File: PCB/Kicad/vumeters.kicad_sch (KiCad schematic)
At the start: 80 parts

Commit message: update elements WIP
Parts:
- D1, D10, D11, D12, D13, D14, D15, D16, D17, D18, D19, D2, D20, D21, D22, D23, D24, D25, D26, D27, D28, D29, D3, D30, D31, D32, D33, D34, D35, D36, D37, D38, D39, D4, D40, D5, D6, D7, D8, D9: renamed from D?; symbol Traktorino-rescue:LED_ALT-Device -> Device:LED_Filled
- gave numbers to parts that had none: 40
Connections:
- net GND: now also D1.1 (K), D10.1 (K), D11.1 (K), D12.1 (K), D13.1 (K), D14.1 (K), D15.1 (K), D16.1 (K), D17.1 (K), D18.1 (K), D19.1 (K), D2.1 (K), D20.1 (K), D21.1 (K), D22.1 (K), D23.1 (K), D24.1 (K), D25.1 (K), D26.1 (K), D27.1 (K), D28.1 (K), D29.1 (K), D3.1 (K), D30.1 (K), D31.1 (K), D32.1 (K), D33.1 (K), D34.1 (K), D35.1 (K), D36.1 (K), D37.1 (K), D38.1 (K), D39.1 (K), D4.1 (K), D40.1 (K), D5.1 (K), D6.1 (K), D7.1 (K), D8.1 (K), D9.1 (K)
- net at R1.2: now also D1.2 (A)
- net at R2.2: now also D2.2 (A)
- net at R3.2: now also D3.2 (A)
- net at R4.2: now also D4.2 (A)
- net at R5.2: now also D5.2 (A)
- net at R6.2: now also D6.2 (A)
- net at R7.2: now also D7.2 (A)
- net at R8.2: now also D8.2 (A)
- net at R16.2: now also D16.2 (A)
- net at R15.2: now also D15.2 (A)
- net at R14.2: now also D14.2 (A)
- net at R13.2: now also D13.2 (A)
- net at R12.2: now also D12.2 (A)
- net at R11.2: now also D11.2 (A)
- net at R10.2: now also D10.2 (A)
- net at R9.2: now also D9.2 (A)
- net at R24.2: now also D24.2 (A)
- net at R23.2: now also D23.2 (A)
- net at R22.2: now also D22.2 (A)
- net at R21.2: now also D21.2 (A)
- net at R20.2: now also D20.2 (A)
- net at R19.2: now also D19.2 (A)
- net at R18.2: now also D18.2 (A)
- net at R17.2: now also D17.2 (A)
- net at R32.2: now also D32.2 (A)
- net at R31.2: now also D31.2 (A)
- net at R30.2: now also D30.2 (A)
- net at R29.2: now also D29.2 (A)
- net at R28.2: now also D28.2 (A)
- net at R27.2: now also D27.2 (A)
- net at R26.2: now also D26.2 (A)
- net at R25.2: now also D25.2 (A)
- net at R40.2: now also D40.2 (A)
- net at R39.2: now also D39.2 (A)
- net at R38.2: now also D38.2 (A)
- net at R37.2: now also D37.2 (A)
- net at R36.2: now also D36.2 (A)
- net at R35.2: now also D35.2 (A)
- net at R34.2: now also D34.2 (A)
- net at R33.2: now also D33.2 (A)

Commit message: progress
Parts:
- added D41, D42, D43, D44, D45, D46, D47: LED_ALT, LED_THT:LED_Rectangular_W3.0mm_H2.0mm, symbol Device:LED_Filled
- added R41, R42, R43, R44, R45, R46, R47: R_Small, Resistor_THT:R_Axial_DIN0207_L6.3mm_D2.5mm_P7.62mm_Horizontal, symbol Device:R_Small
- D1: value LED_ALT -> VUL1-0; footprint (none) -> LED_THT:LED_Rectangular_W3.0mm_H2.0mm
- D10, D11, D12, D13, D14, D15, D16, D9: value LED_ALT -> VUL2; footprint (none) -> LED_THT:LED_Rectangular_W3.0mm_H2.0mm
- D17, D18, D19, D20, D21, D22, D23, D24: value LED_ALT -> VUL3; footprint (none) -> LED_THT:LED_Rectangular_W3.0mm_H2.0mm
- D2: value LED_ALT -> VUL1-1; footprint (none) -> LED_THT:LED_Rectangular_W3.0mm_H2.0mm
- D25, D26, D27, D28, D29, D30, D31, D32: value LED_ALT -> VUMAS-L; footprint (none) -> LED_THT:LED_Rectangular_W3.0mm_H2.0mm
- D3, D4, D5, D6, D7, D8: value LED_ALT -> VUL1-; footprint (none) -> LED_THT:LED_Rectangular_W3.0mm_H2.0mm
- D33, D34, D35, D36, D37, D38, D39, D40: value LED_ALT -> VUMAS-R; footprint (none) -> LED_THT:LED_Rectangular_W3.0mm_H2.0mm
- R1, R10, R11, R12, R13, R14, R15, R16, R17, R18, R19, R2, R20, R21, R22, R23, R24, R25, R26, R27, R28, R29, R3, R30, R31, R32, R33, R34, R35, R36, R37, R38, R39, R4, R40, R5, R6, R7, R8, R9: footprint (none) -> Resistor_THT:R_Axial_DIN0207_L6.3mm_D2.5mm_P7.62mm_Horizontal
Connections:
- net GND: now also D41.1 (K), D42.1 (K), D43.1 (K), D44.1 (K), D45.1 (K), D46.1 (K), D47.1 (K)
- net VULMASL-0 renamed VUMASL-0
- net VULMASL-1 renamed VUMASL-1
- net VULMASL-2 renamed VUMASL-2
- net VULMASL-3 renamed VUMASL-3
- net VULMASL-4 renamed VUMASL-4
- net VULMASL-5 renamed VUMASL-5
- net VULMASL-6 renamed VUMASL-6
- net VULMASL-7 renamed VUMASL-7
- new net: D44.2 (A), R44.2
- new net: D42.2 (A), R42.2
- new net: D47.2 (A), R47.2
- new net: D45.2 (A), R45.2
- new net: D43.2 (A), R43.2
- new net: D46.2 (A), R46.2
- new net: D41.2 (A), R41.2
- new net LEDCUEL: R44.1
- new net LEDCUER: R42.1
- new net LEDHPL1: R47.1
- new net LEDHPL2: R46.1
- new net LEDHPL3: R45.1
- new net LEDPLAYL: R43.1
- new net LEDPLAYR: R41.1
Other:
- moved on the sheet: D1, D10, D11, D12, D13, D14, D15, D16, D17, D18, D19, D2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

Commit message: mod layout
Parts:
- renumbered D42 to D10, D43 to D11, D44 to D12, D9 to D13, D10 to D14, D11 to D15, D12 to D16, D13 to D17, D14 to D18, D15 to D19, D16 to D20, D45 to D21, D46 to D22, D47 to D23, D17 to D24, D18 to D25, D19 to D26, D20 to D27, D21 to D28, D22 to D29, D23 to D30, D24 to D31, D25 to D32, D26 to D33, D27 to D34, D28 to D35, D29 to D36, D30 to D37, D31 to D38, D32 to D39, D33 to D40, D34 to D41, D35 to D42, D36 to D43, D37 to D44, D38 to D45, D39 to D46, D40 to D47, D41 to D9, R42 to R10, R43 to R11, R44 to R12, R9 to R13, R10 to R14, R11 to R15, R12 to R16, R13 to R17, R14 to R18, R15 to R19, R16 to R20, R45 to R21, R46 to R22, R47 to R23, R17 to R24, R18 to R25, R19 to R26, R20 to R27, R21 to R28, R22 to R29, R23 to R30, R24 to R31, R25 to R32, R26 to R33, R27 to R34, R28 to R35, R29 to R36, R30 to R37, R31 to R38, R32 to R39, R33 to R40, R34 to R41, R35 to R42, R36 to R43, R37 to R44, R38 to R45, R39 to R46, R40 to R47, R41 to R9

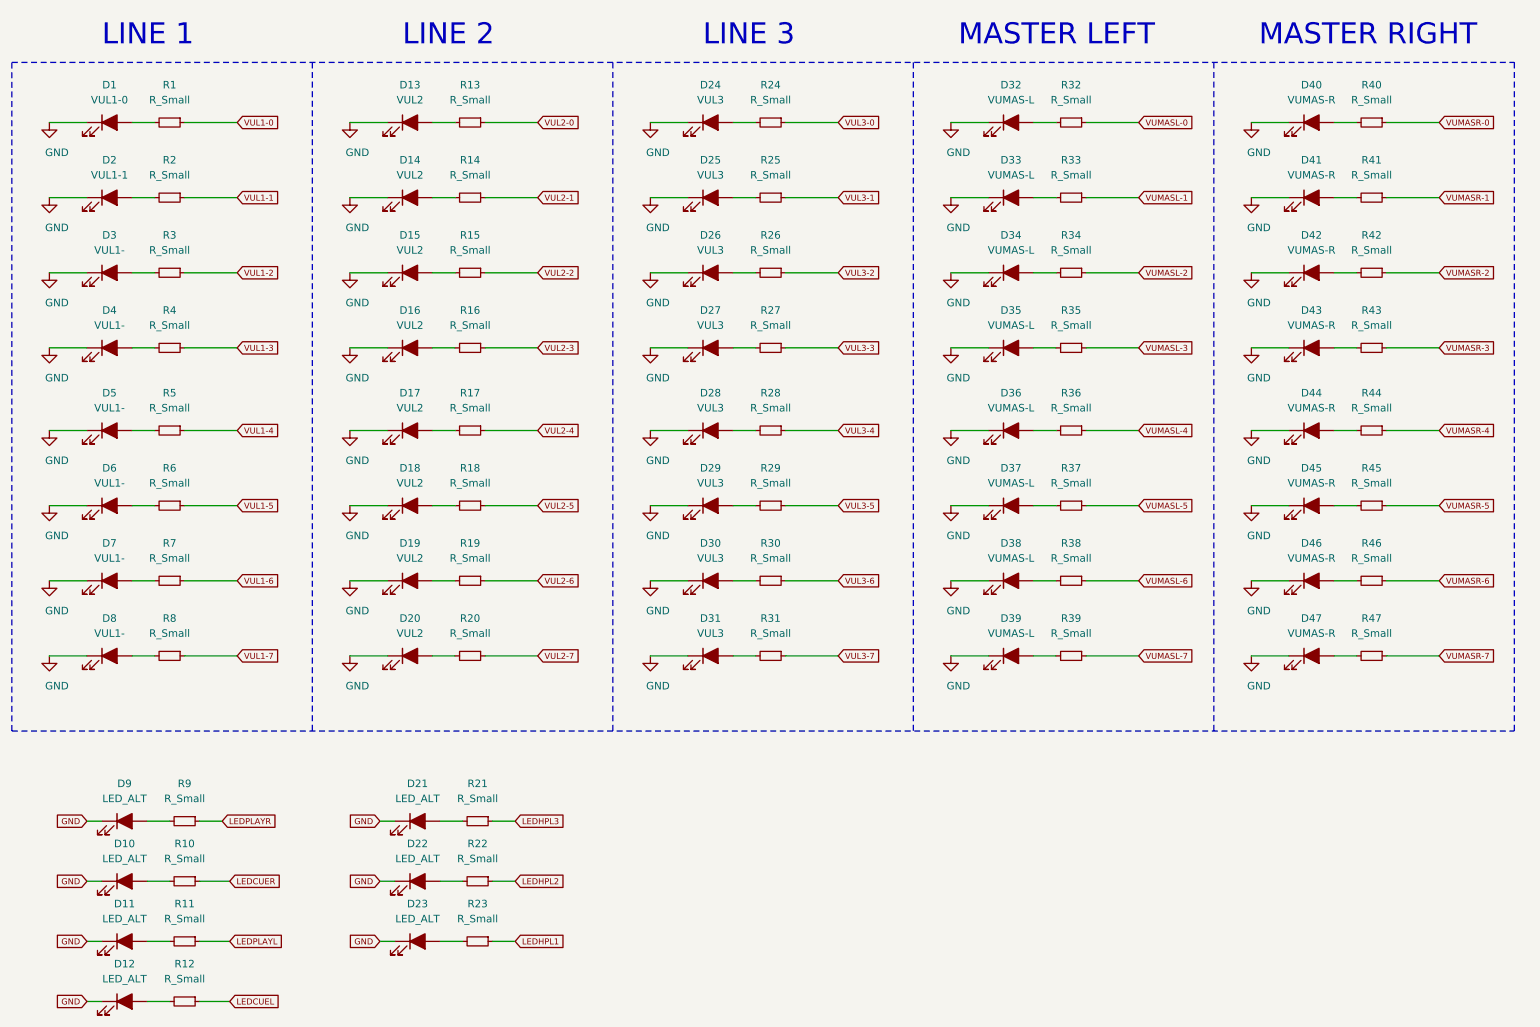
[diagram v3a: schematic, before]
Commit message: Arduino mega retrofit WIP
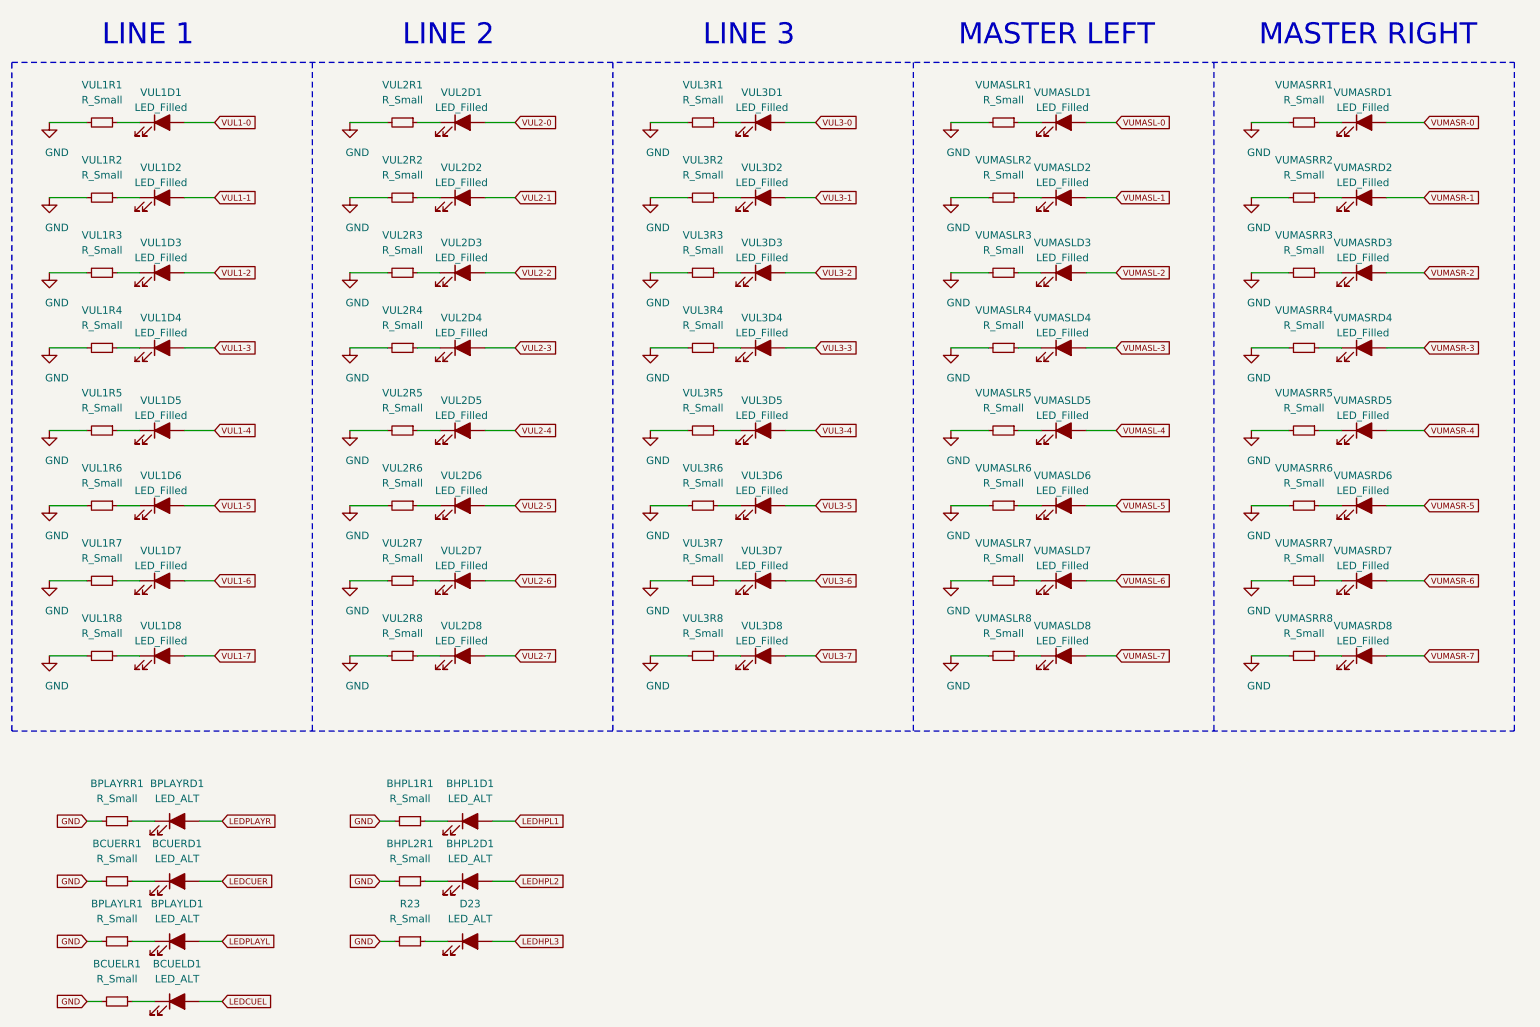
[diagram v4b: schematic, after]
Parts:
- removed D1: VUL1-0, LED_THT:LED_Rectangular_W3.0mm_H2.0mm, symbol Device:LED_Filled
- removed D13, D14, D15, D16, D17, D18, D19, D20: VUL2, LED_THT:LED_Rectangular_W3.0mm_H2.0mm, symbol Device:LED_Filled
- removed D2: VUL1-1, LED_THT:LED_Rectangular_W3.0mm_H2.0mm, symbol Device:LED_Filled
- removed D24, D25, D26, D27, D28, D29, D30, D31: VUL3, LED_THT:LED_Rectangular_W3.0mm_H2.0mm, symbol Device:LED_Filled
- removed D3, D4, D5, D6, D7, D8: VUL1-, LED_THT:LED_Rectangular_W3.0mm_H2.0mm, symbol Device:LED_Filled
- removed D32, D33, D34, D35, D36, D37, D38, D39: VUMAS-L, LED_THT:LED_Rectangular_W3.0mm_H2.0mm, symbol Device:LED_Filled
- removed D40, D41, D42, D43, D44, D45, D46, D47: VUMAS-R, LED_THT:LED_Rectangular_W3.0mm_H2.0mm, symbol Device:LED_Filled
- removed R13, R14, R15, R16, R17, R18, R19, R2, R20, R24, R25, R26, R27, R28, R29, R3, R30, R31, R32, R33, R34, R35, R36, R37, R38, R39, R4, R40, R41, R42, R43, R44, R45, R46, R47, R5, R6, R7, R8: R_Small, Resistor_THT:R_Axial_DIN0207_L6.3mm_D2.5mm_P7.62mm_Horizontal, symbol Device:R_Small
- added VUL1D1, VUL1D2, VUL1D3, VUL1D4, VUL1D5, VUL1D6, VUL1D7, VUL1D8, VUL2D1, VUL2D2, VUL2D3, VUL2D4, VUL2D5, VUL2D6, VUL2D7, VUL2D8, VUL3D1, VUL3D2, VUL3D3, VUL3D4, VUL3D5, VUL3D6, VUL3D7, VUL3D8, VUMASLD1, VUMASLD2, VUMASLD3, VUMASLD4, VUMASLD5, VUMASLD6, VUMASLD7, VUMASLD8, VUMASRD1, VUMASRD2, VUMASRD3, VUMASRD4, VUMASRD5, VUMASRD6, VUMASRD7, VUMASRD8: LED_Filled, LED_THT:LED_Rectangular_W3.0mm_H2.0mm, symbol Device:LED_Filled
- added VUL1R2, VUL1R3, VUL1R4, VUL1R5, VUL1R6, VUL1R7, VUL1R8, VUL2R1, VUL2R2, VUL2R3, VUL2R4, VUL2R5, VUL2R6, VUL2R7, VUL2R8, VUL3R1, VUL3R2, VUL3R3, VUL3R4, VUL3R5, VUL3R6, VUL3R7, VUL3R8, VUMASLR1, VUMASLR2, VUMASLR3, VUMASLR4, VUMASLR5, VUMASLR6, VUMASLR7, VUMASLR8, VUMASRR1, VUMASRR2, VUMASRR3, VUMASRR4, VUMASRR5, VUMASRR6, VUMASRR7, VUMASRR8: R_Small, Resistor_SMD:R_1206_3216Metric_Pad1.30x1.75mm_HandSolder, symbol Device:R_Small
- BCUELR1: renamed from R12; footprint Resistor_THT:R_Axial_DIN0207_L6.3mm_D2.5mm_P7.62mm_Horizontal -> Resistor_SMD:R_1206_3216Metric_Pad1.30x1.75mm_HandSolder
- BCUERR1: renamed from R10; footprint Resistor_THT:R_Axial_DIN0207_L6.3mm_D2.5mm_P7.62mm_Horizontal -> Resistor_SMD:R_1206_3216Metric_Pad1.30x1.75mm_HandSolder
- BHPL1R1: renamed from R21; footprint Resistor_THT:R_Axial_DIN0207_L6.3mm_D2.5mm_P7.62mm_Horizontal -> Resistor_SMD:R_1206_3216Metric_Pad1.30x1.75mm_HandSolder
- BHPL2R1: renamed from R22; footprint Resistor_THT:R_Axial_DIN0207_L6.3mm_D2.5mm_P7.62mm_Horizontal -> Resistor_SMD:R_1206_3216Metric_Pad1.30x1.75mm_HandSolder
- BPLAYLR1: renamed from R11; footprint Resistor_THT:R_Axial_DIN0207_L6.3mm_D2.5mm_P7.62mm_Horizontal -> Resistor_SMD:R_1206_3216Metric_Pad1.30x1.75mm_HandSolder
- BPLAYRR1: renamed from R9; footprint Resistor_THT:R_Axial_DIN0207_L6.3mm_D2.5mm_P7.62mm_Horizontal -> Resistor_SMD:R_1206_3216Metric_Pad1.30x1.75mm_HandSolder
- VUL1R1: renamed from R1; footprint Resistor_THT:R_Axial_DIN0207_L6.3mm_D2.5mm_P7.62mm_Horizontal -> Resistor_SMD:R_1206_3216Metric_Pad1.30x1.75mm_HandSolder
- renumbered D12 to BCUELD1, D10 to BCUERD1, D21 to BHPL1D1, D22 to BHPL2D1, D11 to BPLAYLD1, D9 to BPLAYRD1
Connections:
- net GND: now also BCUELR1.2, BCUERR1.2, BHPL1R1.2, BHPL2R1.2, BPLAYLR1.2, BPLAYRR1.2, R23.2, VUL1R1.2, VUL1R2.2, VUL1R3.2, VUL1R4.2, VUL1R5.2, VUL1R6.2, VUL1R7.2, VUL1R8.2, VUL2R1.2, VUL2R2.2, VUL2R3.2, VUL2R4.2, VUL2R5.2, VUL2R6.2, VUL2R7.2, VUL2R8.2, VUL3R1.2, VUL3R2.2, VUL3R3.2, VUL3R4.2, VUL3R5.2, VUL3R6.2, VUL3R7.2, VUL3R8.2, VUMASLR1.2, VUMASLR2.2, VUMASLR3.2, VUMASLR4.2, VUMASLR5.2, VUMASLR6.2, VUMASLR7.2, VUMASLR8.2, VUMASRR1.2, VUMASRR2.2, VUMASRR3.2, VUMASRR4.2, VUMASRR5.2, VUMASRR6.2, VUMASRR7.2, VUMASRR8.2; no longer BCUELD1.1 (K), BCUERD1.1 (K), BHPL1D1.1 (K), BHPL2D1.1 (K), BPLAYLD1.1 (K), BPLAYRD1.1 (K), D23.1 (K)
- net LEDCUEL: now also BCUELD1.2 (A); no longer BCUELR1.1
- net LEDCUER: now also BCUERD1.2 (A); no longer BCUERR1.1
- net LEDHPL1: now also BHPL1D1.2 (A); no longer R23.1
- net LEDHPL2: now also BHPL2D1.2 (A); no longer BHPL2R1.1
- net LEDHPL3: now also D23.2 (A); no longer BHPL1R1.1
- net LEDPLAYL: now also BPLAYLD1.2 (A); no longer BPLAYLR1.1
- net LEDPLAYR: now also BPLAYRD1.2 (A); no longer BPLAYRR1.1
- net VUL1-0: now also VUL1D1.2 (A); no longer VUL1R1.1
- net VUL1-1: now also VUL1D2.2 (A)
- net VUL1-2: now also VUL1D3.2 (A)
- net VUL1-3: now also VUL1D4.2 (A)
- net VUL1-4: now also VUL1D5.2 (A)
- net VUL1-5: now also VUL1D6.2 (A)
- net VUL1-6: now also VUL1D7.2 (A)
- net VUL1-7: now also VUL1D8.2 (A)
- net VUL2-0: now also VUL2D1.2 (A)
- net VUL2-1: now also VUL2D2.2 (A)
- net VUL2-2: now also VUL2D3.2 (A)
- net VUL2-3: now also VUL2D4.2 (A)
- net VUL2-4: now also VUL2D5.2 (A)
- net VUL2-5: now also VUL2D6.2 (A)
- net VUL2-6: now also VUL2D7.2 (A)
- net VUL2-7: now also VUL2D8.2 (A)
- net VUL3-0: now also VUL3D1.2 (A)
- net VUL3-1: now also VUL3D2.2 (A)
- net VUL3-2: now also VUL3D3.2 (A)
- net VUL3-3: now also VUL3D4.2 (A)
- net VUL3-4: now also VUL3D5.2 (A)
- net VUL3-5: now also VUL3D6.2 (A)
- net VUL3-6: now also VUL3D7.2 (A)
- net VUL3-7: now also VUL3D8.2 (A)
- net VUMASL-0: now also VUMASLD1.2 (A)
- net VUMASL-1: now also VUMASLD2.2 (A)
- net VUMASL-2: now also VUMASLD3.2 (A)
- net VUMASL-3: now also VUMASLD4.2 (A)
- net VUMASL-4: now also VUMASLD5.2 (A)
- net VUMASL-5: now also VUMASLD6.2 (A)
- net VUMASL-6: now also VUMASLD7.2 (A)
- net VUMASL-7: now also VUMASLD8.2 (A)
- net VUMASR-0: now also VUMASRD1.2 (A)
- net VUMASR-1: now also VUMASRD2.2 (A)
- net VUMASR-2: now also VUMASRD3.2 (A)
- net VUMASR-3: now also VUMASRD4.2 (A)
- net VUMASR-4: now also VUMASRD5.2 (A)
- net VUMASR-5: now also VUMASRD6.2 (A)
- net VUMASR-6: now also VUMASRD7.2 (A)
- net VUMASR-7: now also VUMASRD8.2 (A)
- new net: VUL1D1.1 (K), VUL1R1.1
- new net: VUL3D6.1 (K), VUL3R6.1
- new net: VUL1D6.1 (K), VUL1R6.1
- new net: BCUELD1.1 (K), BCUELR1.1
- new net: VUL3D1.1 (K), VUL3R1.1
- new net: VUL3D8.1 (K), VUL3R8.1
- new net: VUL2D2.1 (K), VUL2R2.1
- new net: VUMASRD6.1 (K), VUMASRR6.1
- new net: VUL2D7.1 (K), VUL2R7.1
- new net: VUL1D5.1 (K), VUL1R5.1
- new net: VUL2D6.1 (K), VUL2R6.1
- new net: BCUERD1.1 (K), BCUERR1.1
- new net: VUL3D2.1 (K), VUL3R2.1
- new net: VUMASRD4.1 (K), VUMASRR4.1
- new net: VUMASRD3.1 (K), VUMASRR3.1
- new net: D23.1 (K), R23.1
- new net: VUMASLD8.1 (K), VUMASLR8.1
- new net: VUMASRD5.1 (K), VUMASRR5.1
- new net: VUL2D3.1 (K), VUL2R3.1
- new net: VUL1D4.1 (K), VUL1R4.1
- new net: VUMASRD2.1 (K), VUMASRR2.1
- new net: VUL1D8.1 (K), VUL1R8.1
- new net: VUMASLD2.1 (K), VUMASLR2.1
- new net: VUMASLD6.1 (K), VUMASLR6.1
- new net: VUL3D5.1 (K), VUL3R5.1
- new net: VUL2D5.1 (K), VUL2R5.1
- new net: BHPL1D1.1 (K), BHPL1R1.1
- new net: VUL1D3.1 (K), VUL1R3.1
- new net: VUL3D7.1 (K), VUL3R7.1
- new net: VUMASLD3.1 (K), VUMASLR3.1
- new net: VUMASRD8.1 (K), VUMASRR8.1
- new net: VUL3D3.1 (K), VUL3R3.1
- new net: VUL1D2.1 (K), VUL1R2.1
- new net: VUL1D7.1 (K), VUL1R7.1
- new net: VUMASLD5.1 (K), VUMASLR5.1
- new net: VUL2D4.1 (K), VUL2R4.1
- new net: VUMASLD1.1 (K), VUMASLR1.1
- new net: VUL2D8.1 (K), VUL2R8.1
- new net: VUMASLD7.1 (K), VUMASLR7.1
- new net: VUMASRD7.1 (K), VUMASRR7.1
- new net: VUL3D4.1 (K), VUL3R4.1
- new net: VUMASRD1.1 (K), VUMASRR1.1
- new net: VUL2D1.1 (K), VUL2R1.1
- new net: BPLAYLD1.1 (K), BPLAYLR1.1
- new net: BHPL2D1.1 (K), BHPL2R1.1
- new net: BPLAYRD1.1 (K), BPLAYRR1.1
- new net: VUMASLD4.1 (K), VUMASLR4.1
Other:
- moved on the sheet: BCUELD1, BCUELR1, BCUERD1, BCUERR1, BHPL1D1, BHPL1R1, BHPL2D1, BHPL2R1, BPLAYLD1, BPLAYLR1, BPLAYRD1, BPLAYRR1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

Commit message: pad footprint updated
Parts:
- R23: footprint Resistor_THT:R_Axial_DIN0207_L6.3mm_D2.5mm_P7.62mm_Horizontal -> Resistor_SMD:R_1206_3216Metric_Pad1.30x1.75mm_HandSolder
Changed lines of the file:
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@@
     (property "Reference" "R23" (id 0) (at 90.17 168.91 90))
     (property "Value" "R_Small" (id 1) (at 90.17 171.45 90))
-    (property "Footprint" "Resistor_THT:R_Axial_DIN0207_L6.3mm_D2.5mm_P7.62mm_Horizontal" (id 2) (at 90.17 175.26 0)
+    (property "Footprint" "Resistor_SMD:R_1206_3216Metric_Pad1.30x1.75mm_HandSolder" (id 2) (at 90.17 175.26 0)
       (effects (font (size 1.27 1.27)) hide)
     )
